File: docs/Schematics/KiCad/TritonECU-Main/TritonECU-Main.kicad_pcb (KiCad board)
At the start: 4 copper layers, 158 x 174 mm, 103 parts, among them J1 EEC-V 104, J301 VR spare, Q101 ISL9V3040S3ST, Q102 ISL9V3040S3ST, Q103 ISL9V3040S3ST, Q104 ISL9V3040S3ST, Q105 ISL9V3040S3ST, Q106 ISL9V3040S3ST, Q107 ISL9V3040S3ST, Q108 ISL9V3040S3ST, Q109 BSS138, Q201 ZXMS6005DGQTA, Q202 ZXMS6005DGQTA, Q203 ZXMS6005DGQTA, Q204 ZXMS6005DGQTA, Q205 ZXMS6005DGQTA, Q206 ZXMS6005DGQTA, Q207 ZXMS6005DGQTA, Q208 ZXMS6005DGQTA, U101 74HCT541, U102 TPS3823A-33DBVR, U301 MAX9926UAEE+T, U302 MAX9926UAEE+T, U303 MAX9926UAEE+T

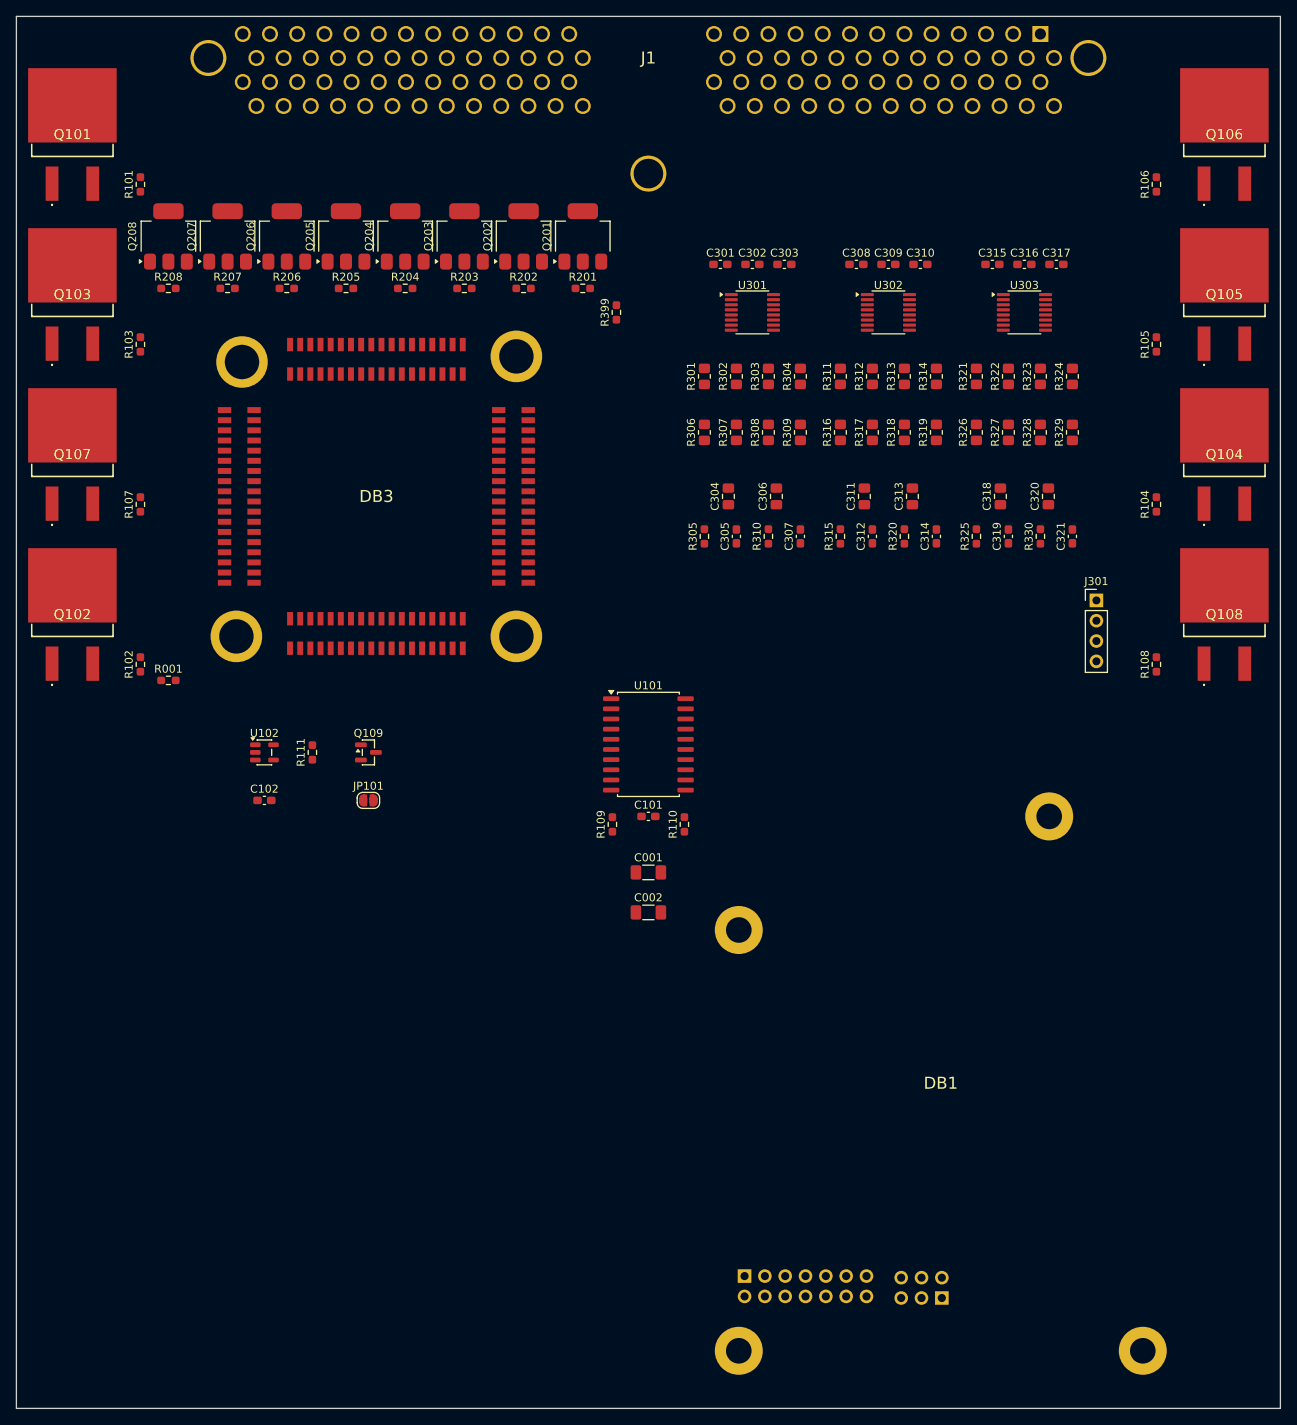
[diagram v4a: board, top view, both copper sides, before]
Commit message: Carrier: Solenoids and PWM sheets, placed on the main board
Solenoids: NCV8405A low-side drivers for the HO2S heaters, vent, IMCC,
SSA/SSB, with 74HCT541 buffering and a 74HC4051 mux for output-sense
dividers. PWM: EVAP, EGR, TCC, EPC, IAC, VSS out, CCS with freewheel
Schottkys (part [CONFIRM]) and supply-sense dividers. ERC 0 errors,
DRC 0 parity issues.

Co-Authored-By: Claude Opus 5.5 <noreply@anthropic.com>
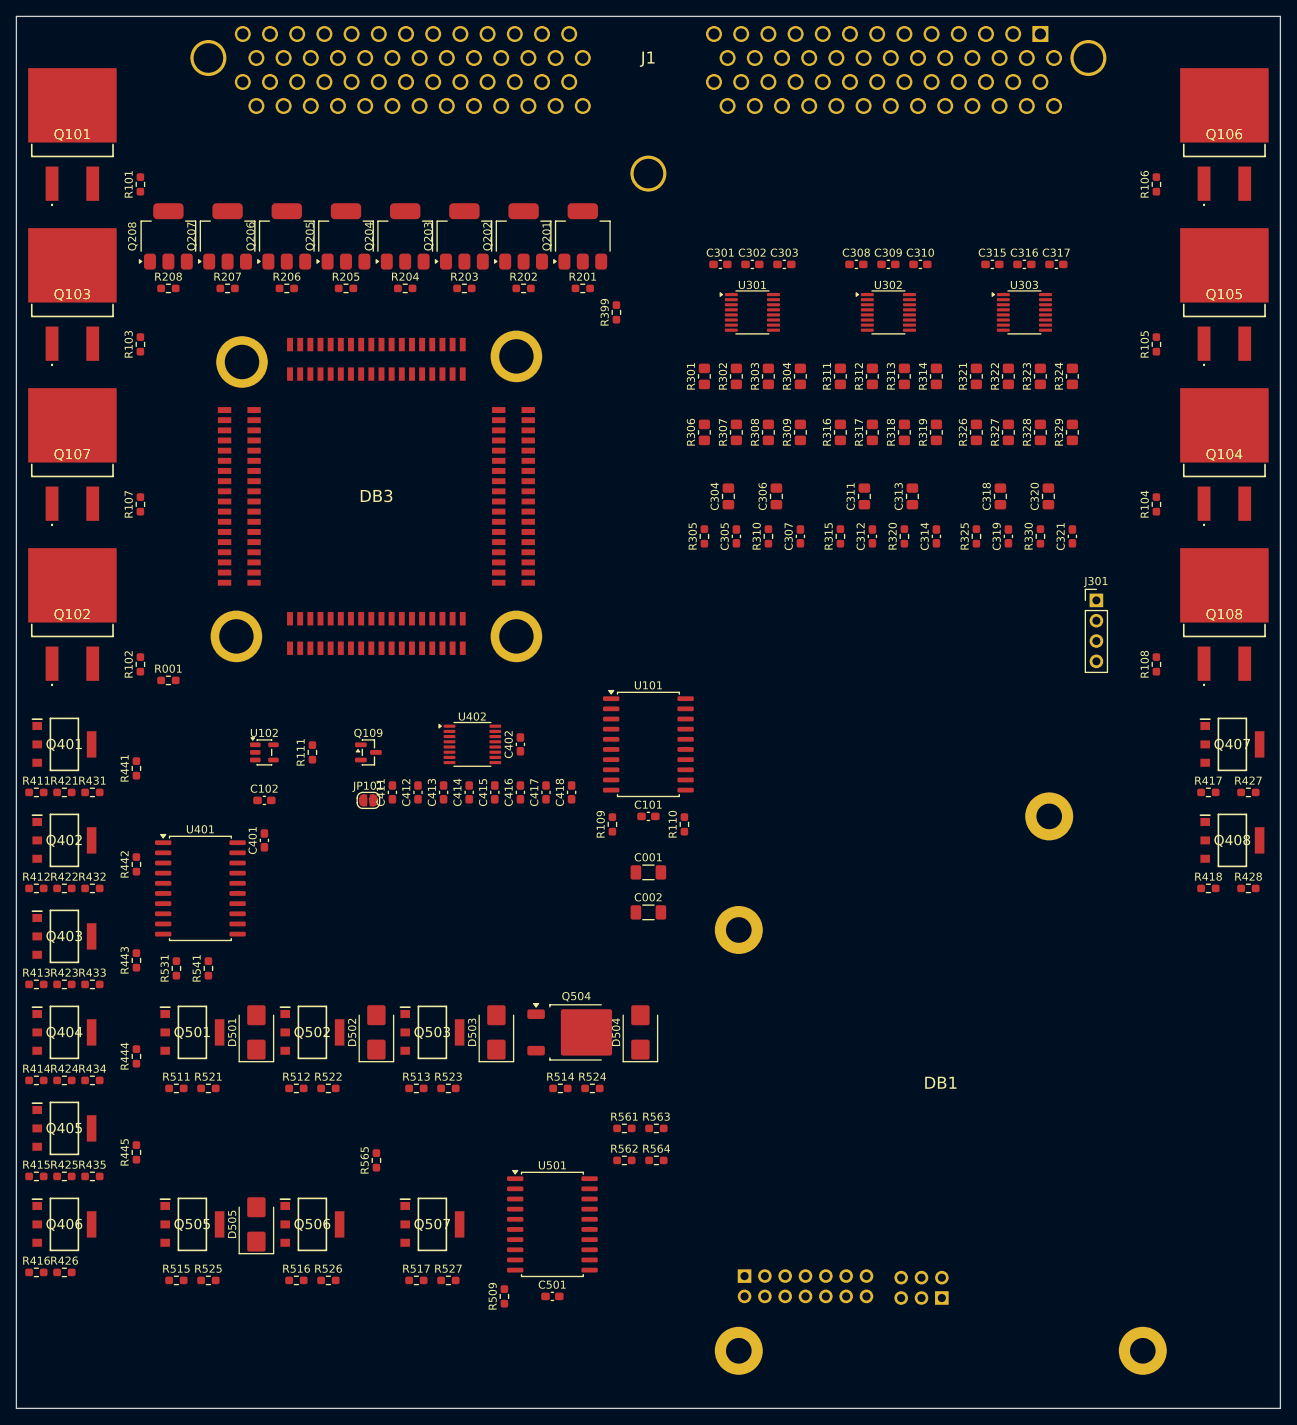
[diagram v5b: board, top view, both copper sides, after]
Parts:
- added C401: 100n, Capacitor_SMD:C_0603_1608Metric_Pad1.08x0.95mm_HandSolder, F.Cu at (56.0, 128.0)
- added C402: 100n, Capacitor_SMD:C_0603_1608Metric_Pad1.08x0.95mm_HandSolder, F.Cu at (88.0, 116.0)
- added C411: 100n, Capacitor_SMD:C_0603_1608Metric_Pad1.08x0.95mm_HandSolder, F.Cu at (72.0, 122.0)
- added C412: 100n, Capacitor_SMD:C_0603_1608Metric_Pad1.08x0.95mm_HandSolder, F.Cu at (75.2, 122.0)
- added C413: 100n, Capacitor_SMD:C_0603_1608Metric_Pad1.08x0.95mm_HandSolder, F.Cu at (78.4, 122.0)
- added C414: 100n, Capacitor_SMD:C_0603_1608Metric_Pad1.08x0.95mm_HandSolder, F.Cu at (81.6, 122.0)
- added C415: 100n, Capacitor_SMD:C_0603_1608Metric_Pad1.08x0.95mm_HandSolder, F.Cu at (84.8, 122.0)
- added C416: 100n, Capacitor_SMD:C_0603_1608Metric_Pad1.08x0.95mm_HandSolder, F.Cu at (88.0, 122.0)
- added C417: 100n, Capacitor_SMD:C_0603_1608Metric_Pad1.08x0.95mm_HandSolder, F.Cu at (91.2, 122.0)
- added C418: 100n, Capacitor_SMD:C_0603_1608Metric_Pad1.08x0.95mm_HandSolder, F.Cu at (94.4, 122.0)
- added C501: 100n, Capacitor_SMD:C_0603_1608Metric_Pad1.08x0.95mm_HandSolder, F.Cu at (92.0, 185.0)
- added D501: STPS3H100UY, Diode_SMD:D_SMB, F.Cu at (55.0, 152.0)
- added D502: STPS3H100UY, Diode_SMD:D_SMB, F.Cu at (70.0, 152.0)
- added D503: STPS3H100UY, Diode_SMD:D_SMB, F.Cu at (85.0, 152.0)
- added D504: STPS3H100UY, Diode_SMD:D_SMB, F.Cu at (103.0, 152.0)
- added D505: STPS3H100UY, Diode_SMD:D_SMB, F.Cu at (55.0, 176.0)
- added Q401: NCV8405ASTT1G, Samacsys:SOT230P700X175-4N, F.Cu at (31.0, 116.0)
- added Q402: NCV8405ASTT1G, Samacsys:SOT230P700X175-4N, F.Cu at (31.0, 128.0)
- added Q403: NCV8405ASTT1G, Samacsys:SOT230P700X175-4N, F.Cu at (31.0, 140.0)
- added Q404: NCV8405ASTT1G, Samacsys:SOT230P700X175-4N, F.Cu at (31.0, 152.0)
- added Q405: NCV8405ASTT1G, Samacsys:SOT230P700X175-4N, F.Cu at (31.0, 164.0)
- added Q406: NCV8405ASTT1G, Samacsys:SOT230P700X175-4N, F.Cu at (31.0, 176.0)
- added Q407: NCV8405ASTT1G, Samacsys:SOT230P700X175-4N, F.Cu at (177.0, 116.0)
- added Q408: NCV8405ASTT1G, Samacsys:SOT230P700X175-4N, F.Cu at (177.0, 128.0)
- added Q501: NCV8405ASTT1G, Samacsys:SOT230P700X175-4N, F.Cu at (47.0, 152.0)
- added Q502: NCV8405ASTT1G, Samacsys:SOT230P700X175-4N, F.Cu at (62.0, 152.0)
- added Q503: NCV8405ASTT1G, Samacsys:SOT230P700X175-4N, F.Cu at (77.0, 152.0)
- added Q504: NCV8408BDTRKG, Package_TO_SOT_SMD:TO-252-2, F.Cu at (95.0, 152.0)
- added Q505: NCV8405ASTT1G, Samacsys:SOT230P700X175-4N, F.Cu at (47.0, 176.0)
- added Q506: NCV8405ASTT1G, Samacsys:SOT230P700X175-4N, F.Cu at (62.0, 176.0)
- added Q507: NCV8405ASTT1G, Samacsys:SOT230P700X175-4N, F.Cu at (77.0, 176.0)
- added R411: 2.2k, Resistor_SMD:R_0603_1608Metric_Pad0.98x0.95mm_HandSolder, F.Cu at (27.5, 122.0)
- added R412: 2.2k, Resistor_SMD:R_0603_1608Metric_Pad0.98x0.95mm_HandSolder, F.Cu at (27.5, 134.0)
- added R413: 2.2k, Resistor_SMD:R_0603_1608Metric_Pad0.98x0.95mm_HandSolder, F.Cu at (27.5, 146.0)
- added R414: 2.2k, Resistor_SMD:R_0603_1608Metric_Pad0.98x0.95mm_HandSolder, F.Cu at (27.5, 158.0)
- added R415: 2.2k, Resistor_SMD:R_0603_1608Metric_Pad0.98x0.95mm_HandSolder, F.Cu at (27.5, 170.0)
- added R416: 2.2k, Resistor_SMD:R_0603_1608Metric_Pad0.98x0.95mm_HandSolder, F.Cu at (27.5, 182.0)
- added R417: 2.2k, Resistor_SMD:R_0603_1608Metric_Pad0.98x0.95mm_HandSolder, F.Cu at (174.0, 122.0)
- added R418: 2.2k, Resistor_SMD:R_0603_1608Metric_Pad0.98x0.95mm_HandSolder, F.Cu at (174.0, 134.0)
- added R421: 100k, Resistor_SMD:R_0603_1608Metric_Pad0.98x0.95mm_HandSolder, F.Cu at (31.0, 122.0)
- added R422: 100k, Resistor_SMD:R_0603_1608Metric_Pad0.98x0.95mm_HandSolder, F.Cu at (31.0, 134.0)
- added R423: 100k, Resistor_SMD:R_0603_1608Metric_Pad0.98x0.95mm_HandSolder, F.Cu at (31.0, 146.0)
- added R424: 100k, Resistor_SMD:R_0603_1608Metric_Pad0.98x0.95mm_HandSolder, F.Cu at (31.0, 158.0)
- added R425: 100k, Resistor_SMD:R_0603_1608Metric_Pad0.98x0.95mm_HandSolder, F.Cu at (31.0, 170.0)
- added R426: 100k, Resistor_SMD:R_0603_1608Metric_Pad0.98x0.95mm_HandSolder, F.Cu at (31.0, 182.0)
- added R427: 100k, Resistor_SMD:R_0603_1608Metric_Pad0.98x0.95mm_HandSolder, F.Cu at (179.0, 122.0)
- added R428: 100k, Resistor_SMD:R_0603_1608Metric_Pad0.98x0.95mm_HandSolder, F.Cu at (179.0, 134.0)
- added R431: 100k, Resistor_SMD:R_0603_1608Metric_Pad0.98x0.95mm_HandSolder, F.Cu at (34.5, 122.0)
- added R432: 100k, Resistor_SMD:R_0603_1608Metric_Pad0.98x0.95mm_HandSolder, F.Cu at (34.5, 134.0)
- added R433: 100k, Resistor_SMD:R_0603_1608Metric_Pad0.98x0.95mm_HandSolder, F.Cu at (34.5, 146.0)
- added R434: 100k, Resistor_SMD:R_0603_1608Metric_Pad0.98x0.95mm_HandSolder, F.Cu at (34.5, 158.0)
- added R435: 100k, Resistor_SMD:R_0603_1608Metric_Pad0.98x0.95mm_HandSolder, F.Cu at (34.5, 170.0)
- added R441: 10.5k, Resistor_SMD:R_0603_1608Metric_Pad0.98x0.95mm_HandSolder, F.Cu at (40.0, 119.0)
- added R442: 10.5k, Resistor_SMD:R_0603_1608Metric_Pad0.98x0.95mm_HandSolder, F.Cu at (40.0, 131.0)
- added R443: 10.5k, Resistor_SMD:R_0603_1608Metric_Pad0.98x0.95mm_HandSolder, F.Cu at (40.0, 143.0)
- added R444: 10.5k, Resistor_SMD:R_0603_1608Metric_Pad0.98x0.95mm_HandSolder, F.Cu at (40.0, 155.0)
- added R445: 10.5k, Resistor_SMD:R_0603_1608Metric_Pad0.98x0.95mm_HandSolder, F.Cu at (40.0, 167.0)
- added R509: 10k, Resistor_SMD:R_0603_1608Metric_Pad0.98x0.95mm_HandSolder, F.Cu at (86.0, 185.0)
- added R511: 2.2k, Resistor_SMD:R_0603_1608Metric_Pad0.98x0.95mm_HandSolder, F.Cu at (45.0, 159.0)
- added R512: 2.2k, Resistor_SMD:R_0603_1608Metric_Pad0.98x0.95mm_HandSolder, F.Cu at (60.0, 159.0)
- added R513: 2.2k, Resistor_SMD:R_0603_1608Metric_Pad0.98x0.95mm_HandSolder, F.Cu at (75.0, 159.0)
- added R514: 2.2k, Resistor_SMD:R_0603_1608Metric_Pad0.98x0.95mm_HandSolder, F.Cu at (93.0, 159.0)
- added R515: 2.2k, Resistor_SMD:R_0603_1608Metric_Pad0.98x0.95mm_HandSolder, F.Cu at (45.0, 183.0)
- added R516: 2.2k, Resistor_SMD:R_0603_1608Metric_Pad0.98x0.95mm_HandSolder, F.Cu at (60.0, 183.0)
- added R517: 2.2k, Resistor_SMD:R_0603_1608Metric_Pad0.98x0.95mm_HandSolder, F.Cu at (75.0, 183.0)
- added R521: 100k, Resistor_SMD:R_0603_1608Metric_Pad0.98x0.95mm_HandSolder, F.Cu at (49.0, 159.0)
- added R522: 100k, Resistor_SMD:R_0603_1608Metric_Pad0.98x0.95mm_HandSolder, F.Cu at (64.0, 159.0)
- added R523: 100k, Resistor_SMD:R_0603_1608Metric_Pad0.98x0.95mm_HandSolder, F.Cu at (79.0, 159.0)
- added R524: 100k, Resistor_SMD:R_0603_1608Metric_Pad0.98x0.95mm_HandSolder, F.Cu at (97.0, 159.0)
- added R525: 100k, Resistor_SMD:R_0603_1608Metric_Pad0.98x0.95mm_HandSolder, F.Cu at (49.0, 183.0)
- added R526: 100k, Resistor_SMD:R_0603_1608Metric_Pad0.98x0.95mm_HandSolder, F.Cu at (64.0, 183.0)
- added R527: 100k, Resistor_SMD:R_0603_1608Metric_Pad0.98x0.95mm_HandSolder, F.Cu at (79.0, 183.0)
- added R531: 100k, Resistor_SMD:R_0603_1608Metric_Pad0.98x0.95mm_HandSolder, F.Cu at (45.0, 144.0)
- added R541: 10.5k, Resistor_SMD:R_0603_1608Metric_Pad0.98x0.95mm_HandSolder, F.Cu at (49.0, 144.0)
- added R561: 100k, Resistor_SMD:R_0603_1608Metric_Pad0.98x0.95mm_HandSolder, F.Cu at (101.0, 164.0)
- added R562: 10.5k, Resistor_SMD:R_0603_1608Metric_Pad0.98x0.95mm_HandSolder, F.Cu at (101.0, 168.0)
- added R563: 100k, Resistor_SMD:R_0603_1608Metric_Pad0.98x0.95mm_HandSolder, F.Cu at (105.0, 164.0)
- added R564: 10.5k, Resistor_SMD:R_0603_1608Metric_Pad0.98x0.95mm_HandSolder, F.Cu at (105.0, 168.0)
- added R565: 10k, Resistor_SMD:R_0603_1608Metric_Pad0.98x0.95mm_HandSolder, F.Cu at (70.0, 168.0)
- added U401: 74HCT541, Package_SO:SOIC-20W_7.5x12.8mm_P1.27mm, F.Cu at (48.0, 134.0)
- added U402: 74HC4051, Package_SO:TSSOP-16_4.4x5mm_P0.65mm, F.Cu at (82.0, 116.0)
- added U501: 74HCT541, Package_SO:SOIC-20W_7.5x12.8mm_P1.27mm, F.Cu at (92.0, 176.0)

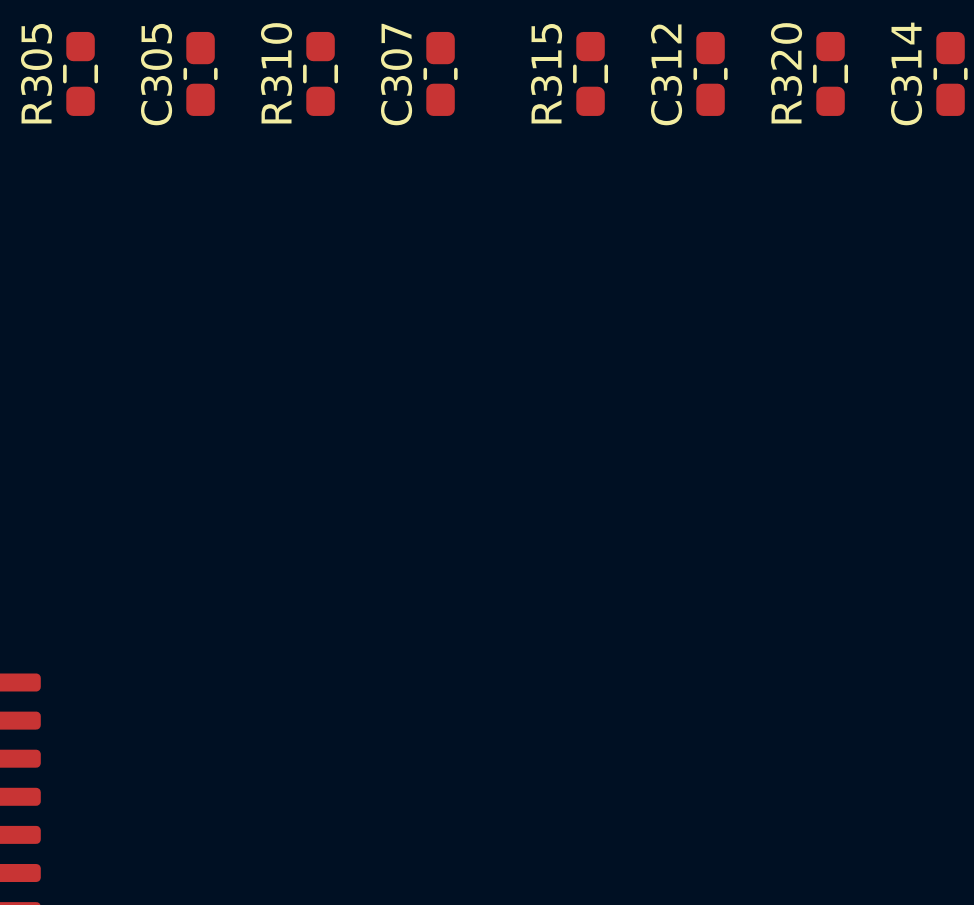
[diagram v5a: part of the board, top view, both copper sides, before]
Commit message: Carrier: Relays sheet (TBD62083AFNG), placed on the main board
FPUMP, FAN1, FAN2, ACC straight from GPIO with 100k pulldowns; PTC per
output (the array has no current limit); COMMON on permanent B+ (pin 55,
[CONFIRM] sharing with the battery-sense divider). Channels 5-8 spare.

Co-Authored-By: Claude Opus 5.5 <noreply@anthropic.com>
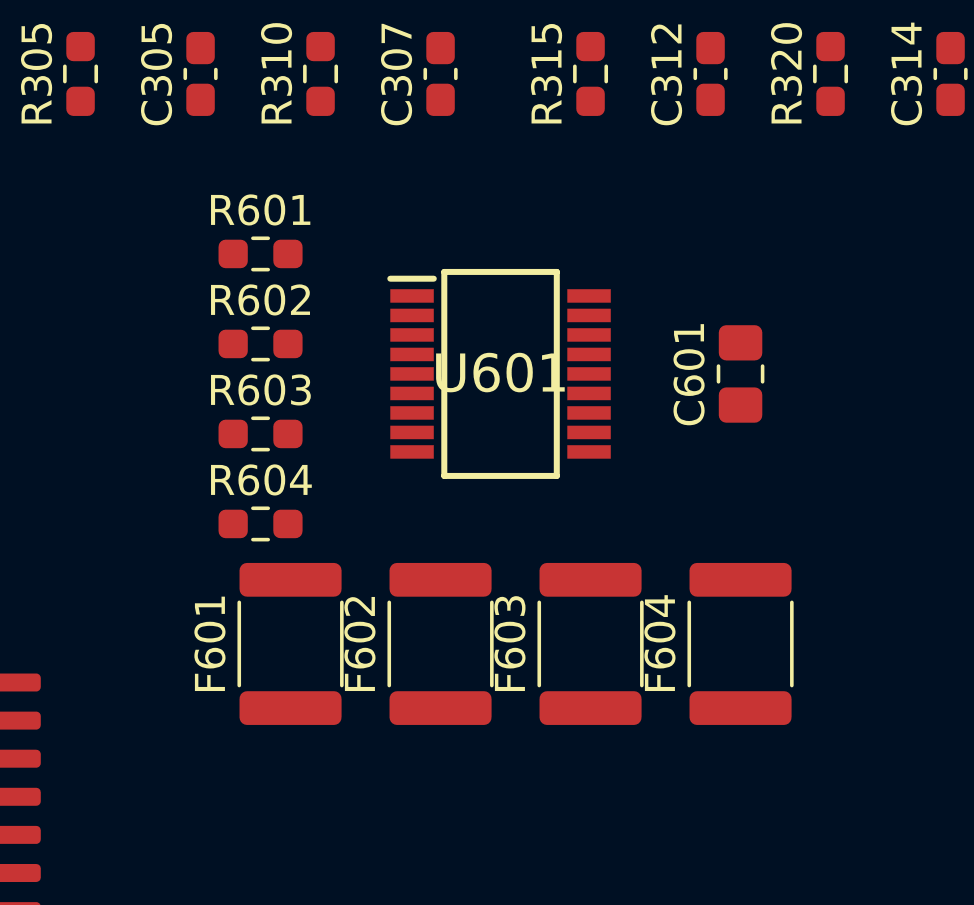
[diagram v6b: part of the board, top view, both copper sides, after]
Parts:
- added C601: 100n, Capacitor_SMD:C_0805_2012Metric_Pad1.18x1.45mm_HandSolder, F.Cu at (133.0, 100.0)
- added F601: MF-MSMF030/60-2, Fuse:Fuse_1812_4532Metric, F.Cu at (118.0, 109.0)
- added F602: MF-MSMF030/60-2, Fuse:Fuse_1812_4532Metric, F.Cu at (123.0, 109.0)
- added F603: MF-MSMF030/60-2, Fuse:Fuse_1812_4532Metric, F.Cu at (128.0, 109.0)
- added F604: MF-MSMF030/60-2, Fuse:Fuse_1812_4532Metric, F.Cu at (133.0, 109.0)
- added R601: 100k, Resistor_SMD:R_0603_1608Metric_Pad0.98x0.95mm_HandSolder, F.Cu at (117.0, 96.0)
- added R602: 100k, Resistor_SMD:R_0603_1608Metric_Pad0.98x0.95mm_HandSolder, F.Cu at (117.0, 99.0)
- added R603: 100k, Resistor_SMD:R_0603_1608Metric_Pad0.98x0.95mm_HandSolder, F.Cu at (117.0, 102.0)
- added R604: 100k, Resistor_SMD:R_0603_1608Metric_Pad0.98x0.95mm_HandSolder, F.Cu at (117.0, 105.0)
- added U601: TBD62083AFNG, Samacsys:SOP65P640X155-18N, F.Cu at (125.0, 100.0)
